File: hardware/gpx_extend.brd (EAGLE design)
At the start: 19.2 x 43 mm, 22 parts, among them SW1 SW-SPST, U1 STM32L011F4PX

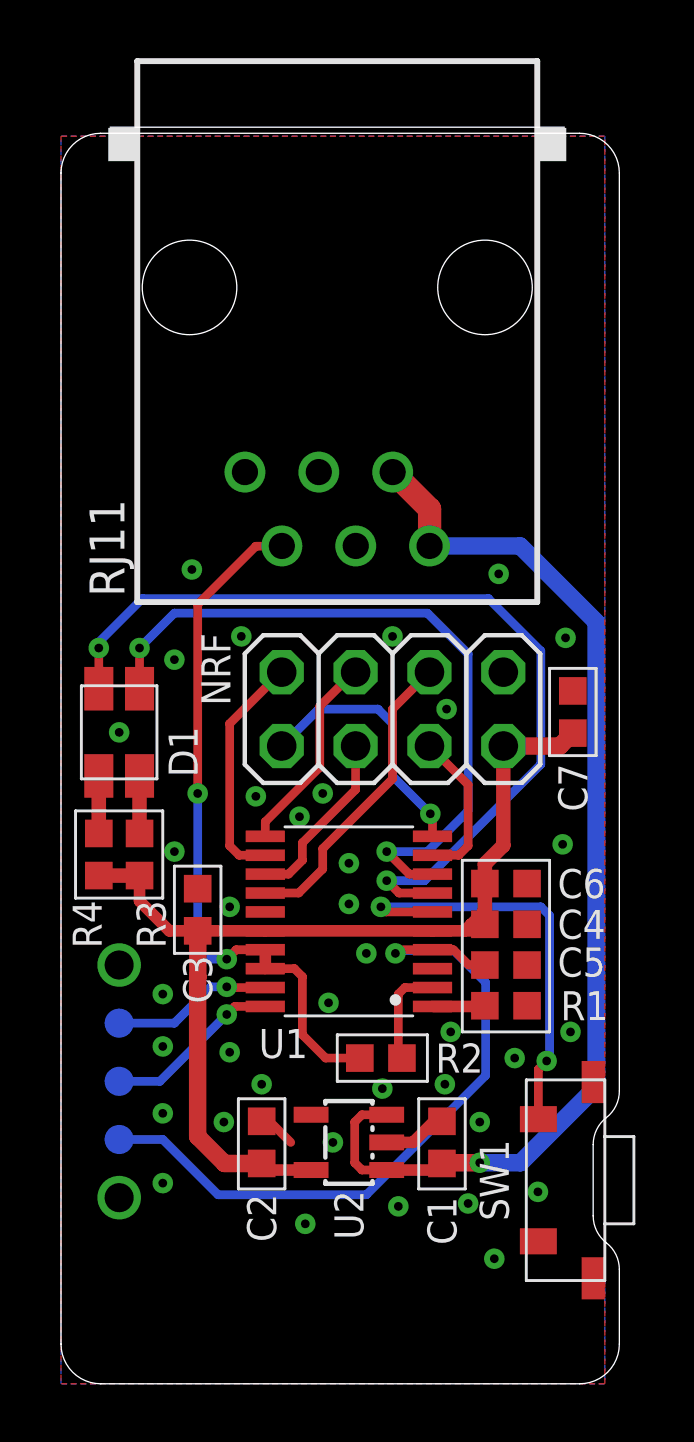
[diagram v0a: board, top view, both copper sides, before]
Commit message: fix DMA transfer bug at lower baudrates
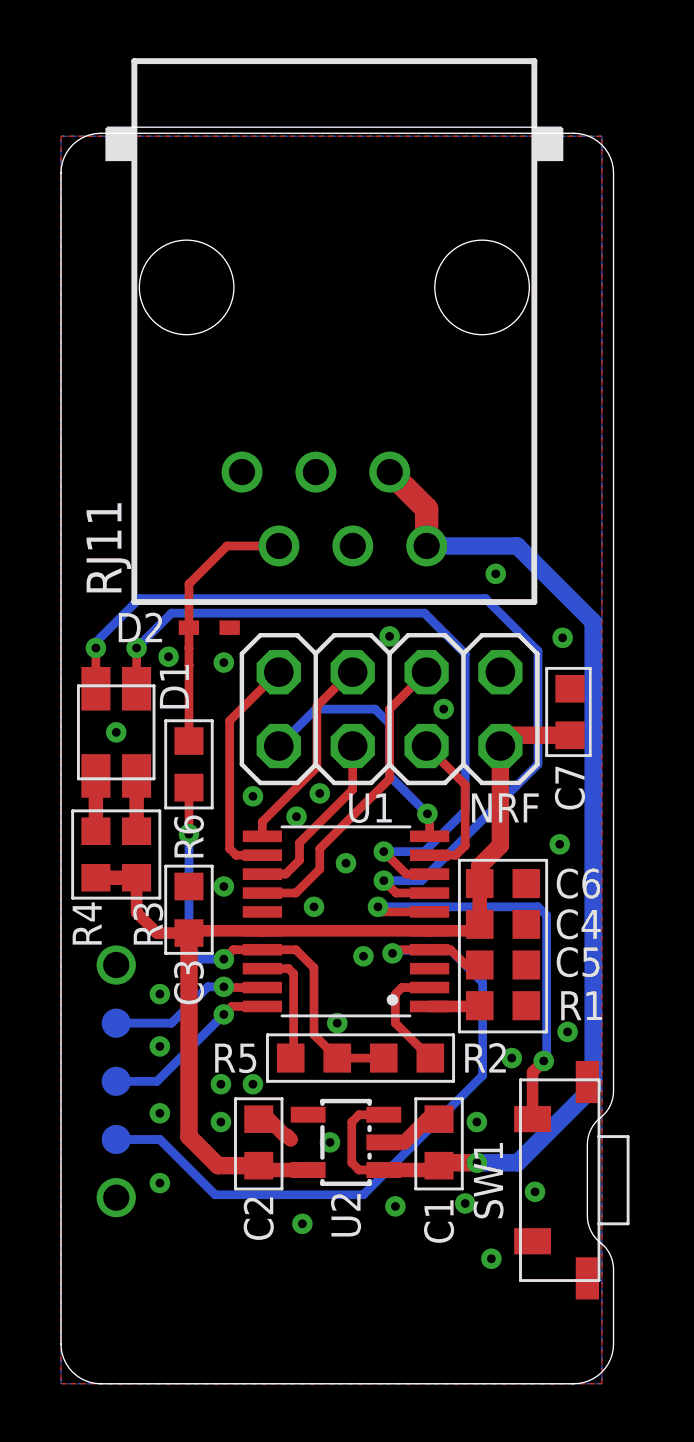
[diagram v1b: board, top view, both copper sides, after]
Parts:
- added D2: UCLAMP3301HSOD523, misc:SOD523
- added R5, R6: 220, misc:0603-MMGRID
- C1, C2, C3, C4, C5, C6, C7: device misc:C0603-S -> misc:0603-MMGRID
- R1, R2, R3, R4: device misc:R0603-S -> misc:0603-MMGRID
- moved R2 0.90 mm to (11.9, 11.2)
- moved C3 0.30 mm to (4.40, 16.3)
- moved SW1 0.20 mm to (17.1, 7.00)
- moved C4 0.10 mm to (15.2, 15.8)
- moved C5 0.10 mm to (15.2, 14.4)
- moved C6 0.10 mm to (15.2, 17.2)
- moved C7 0.10 mm to (17.5, 23.1)
- moved R1 0.10 mm to (15.2, 13.0)
- moved C2 0.10 mm to (6.80, 8.30)
- moved C 0.10 mm to (1.90, 10.4)
- moved D 0.10 mm to (1.90, 12.4)
- moved D1 0.10 mm to (1.90, 22.4)
- moved R 0.10 mm to (1.90, 8.40)
- moved R3 0.10 mm to (2.60, 18.2)
- moved R4 0.10 mm to (1.20, 18.2)
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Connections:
- new net N$1: D2.C, R6.1, RJ11.5
- new net RX: R5.2, U1.P$18
- net D_IO: now also R5.1, R6.2; no longer RJ11.5, U1.P$18
- net GND: now also D2.A
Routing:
- net D_IO: track 24.6 -> 15.4 mm
- net N$1: track 0.00 -> 9.04 mm
- net RX: track 0.00 -> 4.09 mm
- net +3V3: track 36.5 -> 35.4 mm
- net GND: track 3.50 -> 3.62 mm, vias 39 -> 34
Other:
- board size 19.2 x 43 mm -> 19 x 43 mm
